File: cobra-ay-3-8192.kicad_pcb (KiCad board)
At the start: 2 copper layers, 95.2 x 50.2 mm, 28 parts, among them J1 C96ABC, J2 Conn_01x10, J4 Conn_Coaxial, J5 Conn_Coaxial, Q1 BC239, U1 AY-3-8192, U2 74LS138, U3 74LS02, U4 74LS00, U5 74LS74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

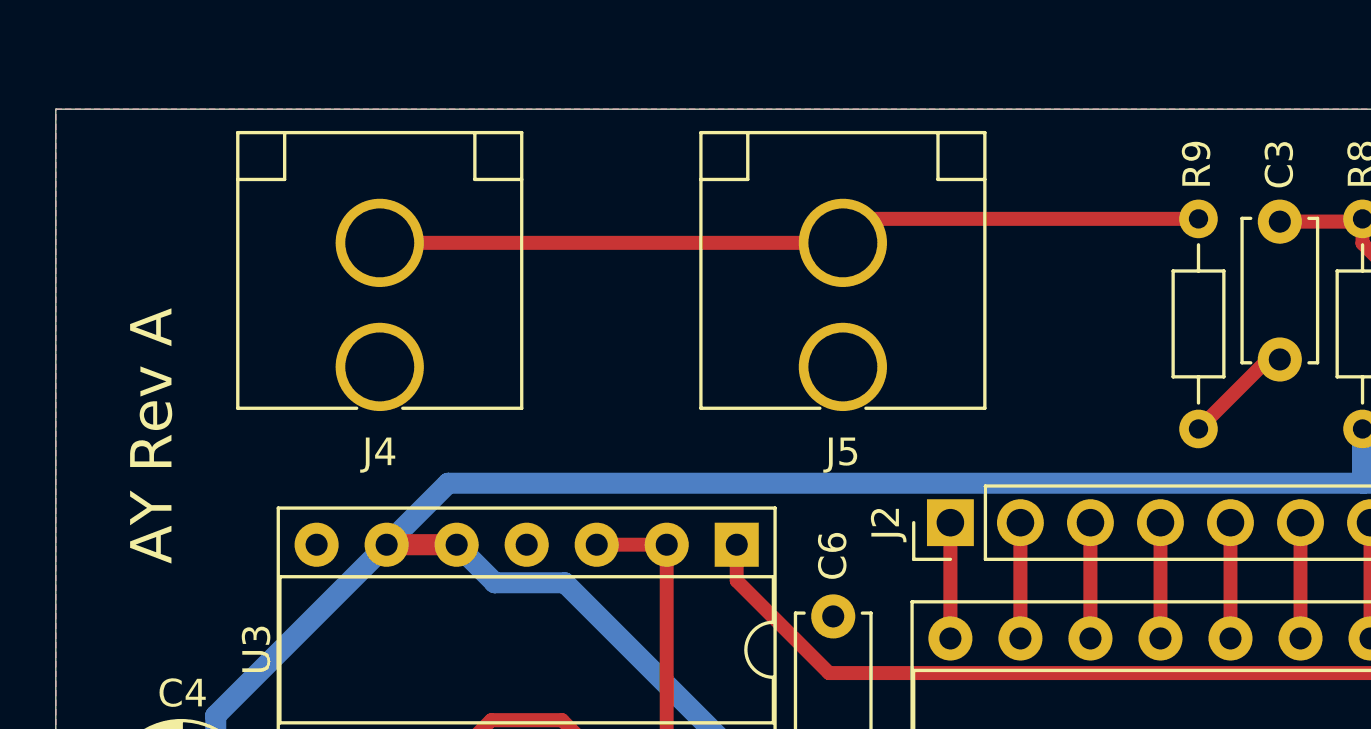
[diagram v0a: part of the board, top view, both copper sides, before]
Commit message: Fix issues with audio input/output
Swap RCA connector pins, move RCA connectors closer to board edge, and
add resistors R10 and R11 to input audio.
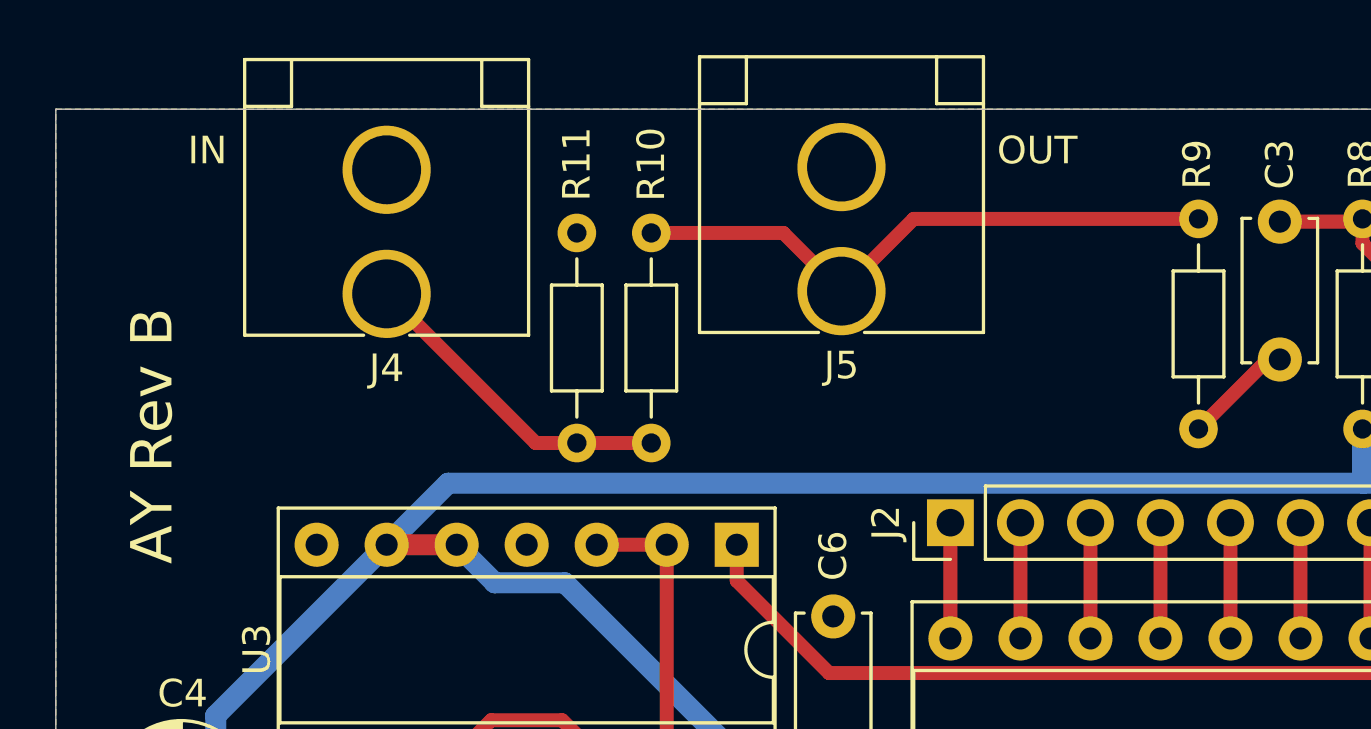
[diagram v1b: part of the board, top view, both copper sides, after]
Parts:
- added R10: 10k, Resistor_THT:R_Axial_DIN0204_L3.6mm_D1.6mm_P7.62mm_Horizontal, F.Cu at (81.6, 105.7)
- added R11: 1K, Resistor_THT:R_Axial_DIN0204_L3.6mm_D1.6mm_P7.62mm_Horizontal, F.Cu at (78.9, 105.7)
- moved J5 2.75 mm to (88.5, 95.7)
- moved J4 2.66 mm to (72.0, 95.8)
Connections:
- J1 pad A1: Net-(J1-PadA1) -> unconnected-(J1-PadA1)
- J1 pad A10: Net-(J1-PadA10) -> unconnected-(J1-PadA10)
- J1 pad A11: Net-(J1-PadA11) -> unconnected-(J1-PadA11)
- J1 pad A13: Net-(J1-PadA13) -> unconnected-(J1-PadA13)
- J1 pad A17: Net-(J1-PadA17) -> unconnected-(J1-PadA17)
- J1 pad A18: Net-(J1-PadA18) -> unconnected-(J1-PadA18)
- J1 pad A19: Net-(J1-PadA19) -> unconnected-(J1-PadA19)
- J1 pad A20: Net-(J1-PadA20) -> unconnected-(J1-PadA20)
- J1 pad A21: Net-(J1-PadA21) -> unconnected-(J1-PadA21)
- J1 pad A22: Net-(J1-PadA22) -> unconnected-(J1-PadA22)
- J1 pad A23: Net-(J1-PadA23) -> unconnected-(J1-PadA23)
- J1 pad A26: Net-(J1-PadA26) -> unconnected-(J1-PadA26)
- J1 pad A27: Net-(J1-PadA27) -> unconnected-(J1-PadA27)
- J1 pad A28: Net-(J1-PadA28) -> unconnected-(J1-PadA28)
- J1 pad A3: Net-(J1-PadA3) -> unconnected-(J1-PadA3)
- J1 pad A30: Net-(J1-PadA30) -> unconnected-(J1-PadA30)
- J1 pad A32: Net-(J1-PadA32) -> unconnected-(J1-PadA32)
- J1 pad A6: Net-(J1-PadA6) -> unconnected-(J1-PadA6)
- J1 pad A7: Net-(J1-PadA7) -> unconnected-(J1-PadA7)
- J1 pad A9: Net-(J1-PadA9) -> unconnected-(J1-PadA9)
- J1 pad B1: Net-(J1-PadB1) -> unconnected-(J1-PadB1)
- J1 pad B10: Net-(J1-PadB10) -> unconnected-(J1-PadB10)
- J1 pad B11: Net-(J1-PadB11) -> unconnected-(J1-PadB11)
- J1 pad B12: Net-(J1-PadB12) -> unconnected-(J1-PadB12)
- J1 pad B13: Net-(J1-PadB13) -> unconnected-(J1-PadB13)
- J1 pad B14: Net-(J1-PadB14) -> unconnected-(J1-PadB14)
- J1 pad B15: Net-(J1-PadB15) -> unconnected-(J1-PadB15)
- J1 pad B16: Net-(J1-PadB16) -> unconnected-(J1-PadB16)
- J1 pad B17: Net-(J1-PadB17) -> unconnected-(J1-PadB17)
- J1 pad B18: Net-(J1-PadB18) -> unconnected-(J1-PadB18)
- J1 pad B19: Net-(J1-PadB19) -> unconnected-(J1-PadB19)
- J1 pad B20: Net-(J1-PadB20) -> unconnected-(J1-PadB20)
- J1 pad B21: Net-(J1-PadB21) -> unconnected-(J1-PadB21)
- J1 pad B22: Net-(J1-PadB22) -> unconnected-(J1-PadB22)
- J1 pad B23: Net-(J1-PadB23) -> unconnected-(J1-PadB23)
- J1 pad B24: Net-(J1-PadB24) -> unconnected-(J1-PadB24)
- J1 pad B25: Net-(J1-PadB25) -> unconnected-(J1-PadB25)
- J1 pad B26: Net-(J1-PadB26) -> unconnected-(J1-PadB26)
- J1 pad B27: Net-(J1-PadB27) -> unconnected-(J1-PadB27)
- J1 pad B28: Net-(J1-PadB28) -> unconnected-(J1-PadB28)
- J1 pad B29: Net-(J1-PadB29) -> unconnected-(J1-PadB29)
- J1 pad B3: Net-(J1-PadB3) -> unconnected-(J1-PadB3)
- J1 pad B30: Net-(J1-PadB30) -> unconnected-(J1-PadB30)
- J1 pad B32: Net-(J1-PadB32) -> unconnected-(J1-PadB32)
- J1 pad B5: Net-(J1-PadB5) -> unconnected-(J1-PadB5)
- J1 pad B6: Net-(J1-PadB6) -> unconnected-(J1-PadB6)
- J1 pad B7: Net-(J1-PadB7) -> unconnected-(J1-PadB7)
- J1 pad B8: Net-(J1-PadB8) -> unconnected-(J1-PadB8)
- J1 pad B9: Net-(J1-PadB9) -> unconnected-(J1-PadB9)
- J1 pad C1: Net-(J1-PadC1) -> unconnected-(J1-PadC1)
- J1 pad C10: Net-(J1-PadC10) -> unconnected-(J1-PadC10)
- J1 pad C11: Net-(J1-PadC11) -> unconnected-(J1-PadC11)
- J1 pad C17: Net-(J1-PadC17) -> unconnected-(J1-PadC17)
- J1 pad C18: Net-(J1-PadC18) -> unconnected-(J1-PadC18)
- J1 pad C19: Net-(J1-PadC19) -> unconnected-(J1-PadC19)
- J1 pad C20: Net-(J1-PadC20) -> unconnected-(J1-PadC20)
- J1 pad C21: Net-(J1-PadC21) -> unconnected-(J1-PadC21)
- J1 pad C22: Net-(J1-PadC22) -> unconnected-(J1-PadC22)
- J1 pad C23: Net-(J1-PadC23) -> unconnected-(J1-PadC23)
- J1 pad C25: Net-(J1-PadC25) -> unconnected-(J1-PadC25)
- J1 pad C26: Net-(J1-PadC26) -> unconnected-(J1-PadC26)
- J1 pad C27: Net-(J1-PadC27) -> unconnected-(J1-PadC27)
- J1 pad C28: Net-(J1-PadC28) -> unconnected-(J1-PadC28)
- J1 pad C29: Net-(J1-PadC29) -> unconnected-(J1-PadC29)
- J1 pad C3: Net-(J1-PadC3) -> unconnected-(J1-PadC3)
- J1 pad C30: Net-(J1-PadC30) -> unconnected-(J1-PadC30)
- J1 pad C32: Net-(J1-PadC32) -> unconnected-(J1-PadC32)
- J1 pad C6: Net-(J1-PadC6) -> unconnected-(J1-PadC6)
- J1 pad C7: Net-(J1-PadC7) -> unconnected-(J1-PadC7)
- J1 pad C8: Net-(J1-PadC8) -> unconnected-(J1-PadC8)
- J1 pad C9: Net-(J1-PadC9) -> unconnected-(J1-PadC9)
- J4 pad 1: Net-(J4-Pad1) -> Net-(R10-Pad1)
- J5 pad 1: Net-(J4-Pad1) -> Net-(J5-Pad1)
- R9 pad 1: Net-(J4-Pad1) -> Net-(J5-Pad1)
- U1 pad 2: Net-(U1-Pad2) -> unconnected-(U1-Pad2)
- U2 pad 13: Net-(U2-Pad13) -> unconnected-(U2-Pad13)
- U2 pad 14: Net-(U2-Pad14) -> unconnected-(U2-Pad14)
- U2 pad 15: Net-(U2-Pad15) -> unconnected-(U2-Pad15)
- U2 pad 7: Net-(U2-Pad7) -> unconnected-(U2-Pad7)
- U2 pad 9: Net-(U2-Pad9) -> unconnected-(U2-Pad9)
- U3 pad 4: Net-(U3-Pad4) -> unconnected-(U3-Pad4)
- U5 pad 10: Net-(U5-Pad10) -> unconnected-(U5-Pad10)
- U5 pad 11: Net-(U5-Pad11) -> unconnected-(U5-Pad11)
- U5 pad 12: Net-(U5-Pad12) -> unconnected-(U5-Pad12)
- U5 pad 13: Net-(U5-Pad13) -> unconnected-(U5-Pad13)
- U5 pad 8: Net-(U5-Pad8) -> unconnected-(U5-Pad8)
- U5 pad 9: Net-(U5-Pad9) -> unconnected-(U5-Pad9)
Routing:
- net Net-(J4-Pad1): track 30.1 -> 0.00 mm
- net Net-(J5-Pad1): track 0.00 -> 21.8 mm
- net Net-(R10-Pad1): track 0.00 -> 11.8 mm
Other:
- board text added: "AY Rev B"
- board text added: "IN"
- board text added: "OUT"
- board text removed: "AY Rev A"
